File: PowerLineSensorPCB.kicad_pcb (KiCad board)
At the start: 4 copper layers, 115 x 47 mm, 248 parts, among them J1 SIM_Card_Shielded, J10 Conn_Coaxial, J11 Conn_Coaxial, J12 Conn_Coaxial, J13 Conn_Coaxial, J14 Conn_01x06_Pin, J15 Conn_01x03_MountingPin, J16 Conn_01x03_MountingPin, J17 Conn_01x03_MountingPin, J2 Micro_SD_Card, J3 Conn_Coaxial, J5 Conn_01x04_Pin, J6 USB_C_Receptacle_USB2.0_16P, J7 Conn_Coaxial, J8 Conn_01x04_Pin, SW1 SW_Push, SW2 SW_Push, SW3 SW_Push, U1 MLX90637, U10 BQ21080YBGR, U11 LM2903, U12 W25Q128JVE, U13 W25Q128JVE, U14 SKY65943-11, U2 ZTPD2210, U3 RP2350A, U4 RT6150BGQW, U5 TMAG5253BAx, U6 nRF9151-LAXX, U7 LIS2HH12, U8 RAK3172-xx-8-SM-xI, U9 P3T1755, Y1 Crystal_GND24

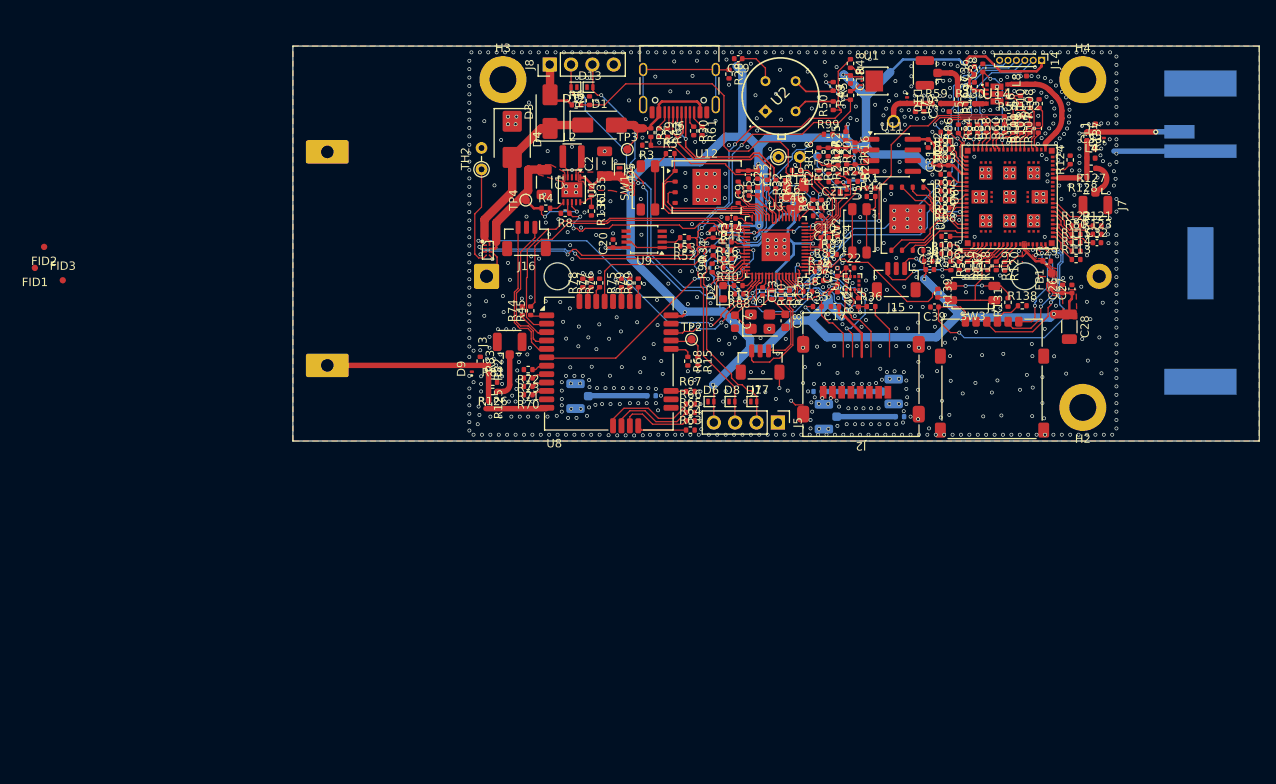
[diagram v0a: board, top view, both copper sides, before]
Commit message: PCB updates
Update miscellaneous.kicad_sch to add new fiducial symbol and replace existing fiducial references

- Added a new fiducial symbol "BC_Miscellaneous:Fiducial" with ground
- Updated references in the schematic to point to the new fiducial symbol.

- Changed the DNP (Do Not Place) property for components U13 and U6 from 'no' to 'yes' to prevent placement on the PCB.
- Updated the footprint property for U13 to "BC_Memory:W25Q" to reflect the correct component footprint.
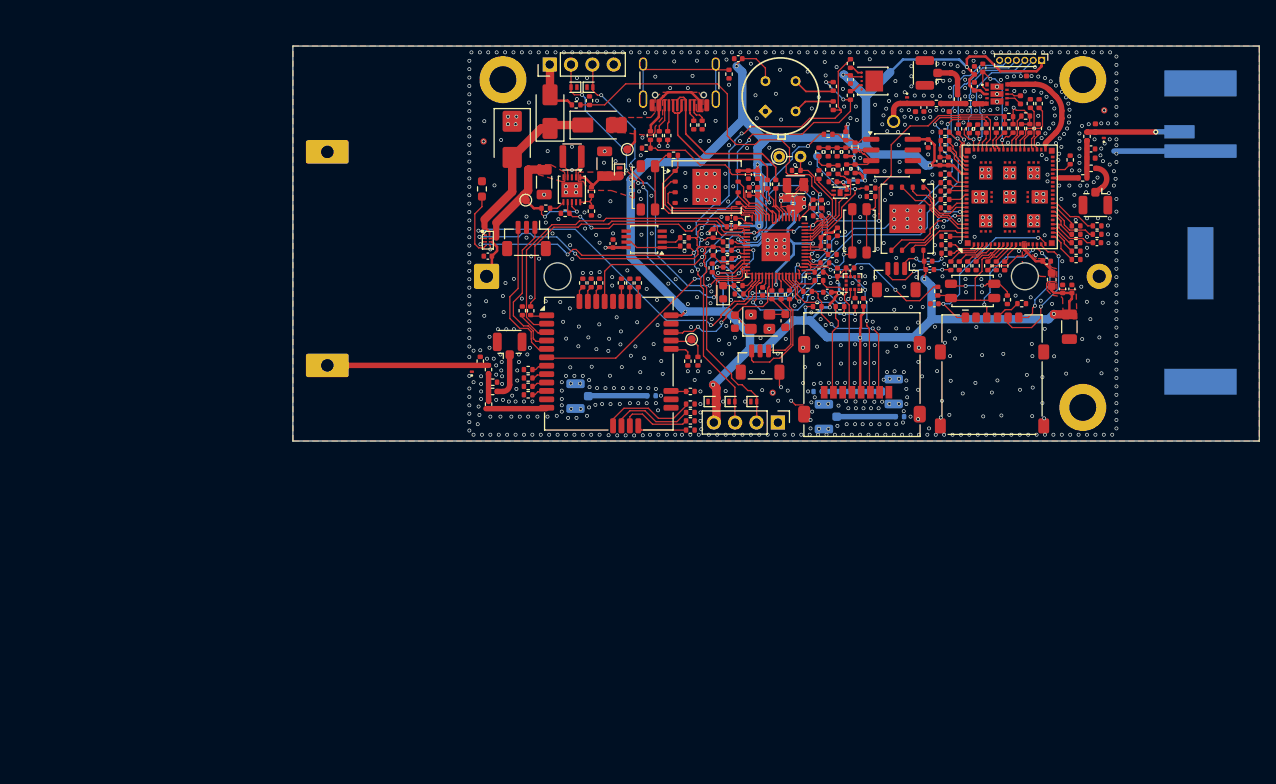
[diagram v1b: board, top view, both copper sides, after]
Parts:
- added C43: 4u7, Capacitor_SMD:C_0402_1005Metric, F.Cu at (123.2, 125.0)
- FID1, FID2, FID3: footprint Fiducial:Fiducial_0.75mm_Mask1.5mm -> BC_Miscellaneous:Fiducial_0.75mm_Mask1.5mm
- J6: footprint Connector_USB:USB_C_Receptacle_HRO_TYPE-C-31-M-12 -> BC_Miscellaneous:USB_C_Receptacle_HRO_TYPE-C-31-M-12
- TH2: footprint Resistor_THT:R_Axial_DIN0204_L3.6mm_D1.6mm_P2.54mm_Vertical -> Resistor_SMD:R_0603_1608Metric_Pad0.98x0.95mm_HandSolder
- U12, U13: footprint Package_SON:WSON-8-1EP_8x6mm_P1.27mm_EP3.4x4.3mm -> BC_Memory:W25Q
- moved FID1 128.6 mm to (196.6, 107.7)
- moved FID3 85.5 mm to (157.1, 141.2)
- moved FID2 53.8 mm to (122.7, 111.3)
- moved R36 3.70 mm to (165.1, 131.0), turned to 180 degrees
- moved C17 3.44 mm to (167.9, 130.5), turned to 90 degrees
- moved TH2 2.33 mm to (122.5, 117.0)
- moved C24 1.30 mm to (163.6, 129.3), turned to 180 degrees
- moved U10 1.20 mm to (123.2, 123.1)
- moved J6 0.84 mm to (146.0, 103.0)
- moved R30 0.70 mm to (147.7, 109.4)
- moved R61 0.70 mm to (148.7, 109.4)
- moved J1 0.50 mm to (183.2, 139.1)
- moved R5 0.45 mm to (145.3, 113.0)
- moved R42 0.40 mm to (166.9, 130.5)
- moved C39 0.38 mm to (176.3, 130.7)
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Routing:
- net /Celluar_GNSS/SIM_1V8: track 34.1 -> 21.0 mm
- net /Celluar_GNSS/SIM_RST: track 21.0 -> 12.6 mm
- net ~{CS}_SDCard: track 10.1 -> 18.1 mm
- net Net-(U10-TS/MR): track 12.1 -> 7.66 mm
- net Net-(D1-A): track 17.4 -> 13.4 mm
- net Net-(J2-DAT0): track 6.70 -> 10.6 mm
- net ~{CS}_Accelerometer: track 21.8 -> 18.7 mm
- net /RP_pico/SPI0.TX: track 16.2 -> 19.2 mm
- net /Power/USB.DP: track 21.5 -> 19.0 mm
- net /RP_pico/SPI0.SCK: track 13.8 -> 16.1 mm, vias 2 -> 0
- net /RP_pico/SPI0.RX: track 14.8 -> 12.7 mm, vias 2 -> 3
- net Pulse_Switch_converter: track 26.9 -> 25.1 mm
- net /Power/USB.DM: track 21.5 -> 19.8 mm, vias 2 -> 0
- net Net-(J6-SBU1): track 1.93 -> 3.31 mm
- net +3.3V: track 322.5 -> 321.2 mm, vias 24 -> 26
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- added copper zone on F.Cu, net Net-(D1-A)
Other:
- board text added: "Celluar"
- board text added: "GNNS"
- board text added: "LORA"

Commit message: Update subproject reference for kicad-libs to latest commit fe3e1e7
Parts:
- removed C43: 4u7, Capacitor_SMD:C_0402_1005Metric
- removed TH2: Thermistor_NTC, Resistor_SMD:R_0603_1608Metric_Pad0.98x0.95mm_HandSolder
- removed U10: BQ21080YBGR, BC_Power:BGA8C40P2X4_100X155X50
- added C44: 4u7, Capacitor_SMD:C_0402_1005Metric, F.Cu at (118.5, 181.9)
- added D14: LED, Diode_SMD:D_0603_1608Metric, F.Cu at (119.2, 179.6)
- added R101: 100R, Resistor_SMD:R_0402_1005Metric, F.Cu at (111.2, 179.3)
- added R102: 10k, Resistor_SMD:R_0402_1005Metric, F.Cu at (111.2, 181.3)
- added R103: 100R, Resistor_SMD:R_0402_1005Metric, F.Cu at (111.2, 183.3)
- added R104: 10k, Resistor_SMD:R_0402_1005Metric, F.Cu at (111.2, 185.3)
- added TH3: Thermistor_NTC, Resistor_SMD:R_0603_1608Metric_Pad0.98x0.95mm_HandSolder, F.Cu at (114.8, 183.6)
- added U15: BQ25186, BC_Power:BQ25186DLHR_SON40P220X200X80-11N, F.Cu at (124.5, 118.7)
- moved TH1 3.37 mm to (160.9, 111.7), turned to -90 degrees
- moved R14 1.00 mm to (160.9, 114.8)
- moved R30 0.50 mm to (148.2, 109.4)
- moved R61 0.50 mm to (149.2, 109.4)
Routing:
- net /Power/IN: track 20.9 -> 9.99 mm
- net +3.3V: track 321.2 -> 330.9 mm
- net Net-(U10-TS/MR): track 7.66 -> 0.00 mm
- net /Power/SYS: track 22.7 -> 15.4 mm
- net Power_ext: track 51.9 -> 48.3 mm
- net Net-(BT1-+): track 5.44 -> 4.29 mm
- net ~{INT}_Battery_Charger: track 42.7 -> 41.5 mm, vias 2 -> 1
- net Net-(D1-A): track 13.4 -> 14.4 mm
- net /I2C0.SDA: track 91.9 -> 91.0 mm, vias 6 -> 5
- net /I2C0.SCL: track 93.8 -> 93.0 mm, vias 6 -> 5
- net /Power/USB.DM: track 19.8 -> 20.5 mm
- net /RP_pico/A3: track 13.1 -> 12.4 mm
- net GND: track 27.4 -> 26.9 mm, vias 924 -> 912
- net Net-(J6-SBU2): track 2.47 -> 2.97 mm

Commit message: pcb updates
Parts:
- moved R103 70.5 mm to (138.7, 118.4), turned to 90 degrees
- moved R104 67.5 mm to (123.6, 119.0)
- moved R102 64.7 mm to (128.1, 118.9), turned to 90 degrees
- moved D14 63.4 mm to (137.4, 118.9), turned to 90 degrees
- moved R101 62.9 mm to (126.6, 118.4)
- moved TH3 62.6 mm to (122.5, 121.5), turned to -90 degrees
- moved C44 57.6 mm to (123.2, 124.5), turned to 180 degrees
- moved R14 18.2 mm to (154.5, 97.8), turned to -90 degrees
- moved TH1 14.2 mm to (160.1, 97.5), turned to 180 degrees
- moved TP4 6.13 mm to (129.9, 112.6)
- moved U15 2.67 mm to (125.6, 116.3)
- moved TP1 1.91 mm to (162.6, 115.0)
- moved R48 0.55 mm to (166.0, 102.5), turned to 0 degrees
- moved D10 0.10 mm to (173.1, 106.4)
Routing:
- net Net-(D14-K): track 0.00 -> 12.8 mm, vias 0 -> 2
- net Net-(BT1-+): track 4.29 -> 17.0 mm, vias 0 -> 3
- net /RP_pico/A3: track 12.4 -> 0.00 mm
- net /I2C0.SDA: track 91.0 -> 100.5 mm, vias 5 -> 6
- net Net-(U15-~{CE}): track 0.00 -> 8.33 mm, vias 0 -> 2
- net /I2C0.SCL: track 93.0 -> 100.0 mm, vias 5 -> 6
- net /Power/SYS: track 15.4 -> 10.2 mm
- net Net-(U15-~{INT}): track 0.00 -> 4.80 mm, vias 0 -> 2
- net Net-(D14-A): track 0.00 -> 1.63 mm
- net /sens1: track 18.0 -> 16.7 mm
- net ~{INT}_Battery_Charger: track 41.5 -> 40.3 mm, vias 1 -> 2
- net Net-(J6-SHIELD): track 18.6 -> 19.6 mm
- net Pulse_Switch_converter: track 25.1 -> 26.0 mm
- net +3.3V: track 330.9 -> 331.5 mm
- net /50Hz: track 53.1 -> 52.5 mm
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- added copper zone on F.Cu, net /Power/IN
- added copper zone on B.Cu, net Net-(BT1-+)
- added copper zone on F.Cu, net Net-(BT1-+)

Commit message: send to production. v0.1, making jobset for export
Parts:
- added H1: MountingHole_Pad, MountingHole:MountingHole_3.2mm_M3_DIN965_Pad, F.Cu at (150.0, 143.0)
- J5: footprint Connector_PinHeader_2.54mm:PinHeader_1x04_P2.54mm_Vertical -> Connector_PinHeader_2.54mm:PinHeader_2x02_P2.54mm_Vertical
- moved R14 15.7 mm to (159.2, 112.8)
- moved TH1 15.3 mm to (163.2, 112.5)
- moved R63 10.9 mm to (149.0, 134.9), turned to 90 degrees
- moved FID3 9.23 mm to (150.7, 134.6)
- moved R1 8.35 mm to (160.8, 114.3), turned to 180 degrees
- moved R64 7.99 mm to (149.8, 137.0), turned to 90 degrees
- moved R65 6.76 mm to (148.8, 137.0), turned to 90 degrees
- moved D6 6.03 mm to (151.4, 136.5)
- moved D7 5.59 mm to (151.4, 137.9)
- moved R66 3.44 mm to (147.8, 139.2), turned to 90 degrees
- moved R19 3.31 mm to (166.7, 117.5)
- moved R17 3.22 mm to (166.7, 116.0), turned to 180 degrees
- moved D8 3.12 mm to (151.4, 139.3)
- moved R18 3.04 mm to (164.9, 114.6)
- moved J5 2.64 mm to (155.1, 144.7), turned to 90 degrees
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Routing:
- net /RP_pico/A3: track 0.00 -> 16.1 mm
- net Net-(U15-TS/MR): track 0.00 -> 9.34 mm, vias 0 -> 2
- net GND: track 26.9 -> 36.2 mm, vias 910 -> 922
- net /LORA/U1: track 5.86 -> 14.5 mm, vias 0 -> 2
- net +3.3V: track 331.5 -> 339.6 mm, vias 26 -> 27
- net /LORA/U2: track 8.67 -> 16.3 mm, vias 0 -> 2
- net /LORA/U3: track 9.99 -> 15.5 mm, vias 0 -> 2
- net /I2C0.SDA: track 100.5 -> 104.3 mm, vias 6 -> 8
- net /LORA/U4: track 11.4 -> 14.3 mm
- net Net-(U4-LX2): track 2.73 -> 0.00 mm
- net Net-(U4-LX1): track 2.71 -> 0.00 mm
- net /Power/SYS: track 10.2 -> 12.2 mm
- net /sens1: track 16.7 -> 15.4 mm, vias 1 -> 2
- net /I2C0.SCL: track 100.0 -> 98.9 mm, vias 6 -> 8
- net Pulse_Switch_converter: track 26.0 -> 25.0 mm
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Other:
- board text added: "Rev: ${REVISION}"
